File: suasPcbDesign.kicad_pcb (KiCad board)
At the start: 4 copper layers, 0 parts

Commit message: Do the layout
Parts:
- added 3xM3: MountingHole_3.2mm_M3, MountingHole:MountingHole_3.2mm_M3, F.Cu at (132.0, 186.0)
- added BBCC1: 1uF, Capacitor_SMD:C_0603_1608Metric_Pad1.08x0.95mm_HandSolder, F.Cu at (127.0, 181.2)
- added BBCC2: 1uF, Capacitor_SMD:C_0603_1608Metric_Pad1.08x0.95mm_HandSolder, F.Cu at (123.9, 181.2)
- added BBCC3: 1uF, Capacitor_SMD:C_0603_1608Metric_Pad1.08x0.95mm_HandSolder, F.Cu at (125.5, 181.2)
- added BBCC4: 0.1uF, Capacitor_SMD:C_0603_1608Metric_Pad1.08x0.95mm_HandSolder, F.Cu at (122.4, 181.2)
- added C1: 10u, Capacitor_SMD:C_0603_1608Metric_Pad1.08x0.95mm_HandSolder, F.Cu at (94.8, 102.3)
- added C2: 0.1u, Capacitor_SMD:C_0603_1608Metric_Pad1.08x0.95mm_HandSolder, F.Cu at (94.8, 98.8)
- added C3: 1u, Capacitor_SMD:C_0603_1608Metric_Pad1.08x0.95mm_HandSolder, F.Cu at (94.5, 112.9)
- added C4: 0.1u, Capacitor_SMD:C_0603_1608Metric_Pad1.08x0.95mm_HandSolder, F.Cu at (118.2, 97.8)
- added CBT1: 0.1uF, Capacitor_SMD:C_0603_1608Metric_Pad1.08x0.95mm_HandSolder, F.Cu at (119.3, 176.3)
- added CIC1: 1uF, Capacitor_SMD:C_0603_1608Metric_Pad1.08x0.95mm_HandSolder, F.Cu at (127.2, 169.5)
- added COC1: 47uF, Capacitor_SMD:C_0603_1608Metric_Pad1.08x0.95mm_HandSolder, F.Cu at (118.3, 157.5)
- added COC2: 47uF, Capacitor_SMD:C_0603_1608Metric_Pad1.08x0.95mm_HandSolder, F.Cu at (118.3, 159.3)
- added COC3: 10uF, Capacitor_SMD:C_0603_1608Metric_Pad1.08x0.95mm_HandSolder, F.Cu at (127.2, 162.9)
- added Cap1: 1uF, Capacitor_SMD:C_0603_1608Metric_Pad1.08x0.95mm_HandSolder, F.Cu at (107.8, 126.1)
- added Cap2: 0.1uF, Capacitor_SMD:C_0603_1608Metric_Pad1.08x0.95mm_HandSolder, F.Cu at (104.4, 128.8)
- added Cap3: 0.1uF, Capacitor_SMD:C_0603_1608Metric_Pad1.08x0.95mm_HandSolder, F.Cu at (102.8, 128.8)
- added Cap4: 0.1uF, Capacitor_SMD:C_0603_1608Metric_Pad1.08x0.95mm_HandSolder, F.Cu at (115.8, 128.8)
- added Cap5: 0.1uF, Capacitor_SMD:C_0603_1608Metric_Pad1.08x0.95mm_HandSolder, F.Cu at (114.1, 128.8)
- added Cap_1: 0.1uF, Capacitor_SMD:C_0603_1608Metric_Pad1.08x0.95mm_HandSolder, F.Cu at (101.1, 133.0)
- added Cap_2: 0.1uF, Capacitor_SMD:C_0603_1608Metric_Pad1.08x0.95mm_HandSolder, F.Cu at (103.1, 133.0)
- added Cap_3: 0.1uF, Capacitor_SMD:C_0603_1608Metric_Pad1.08x0.95mm_HandSolder, F.Cu at (101.1, 136.8)
- added Cap_4: 0.1uF, Capacitor_SMD:C_0603_1608Metric_Pad1.08x0.95mm_HandSolder, F.Cu at (103.1, 136.8)
- added Cap_5: 1u, Capacitor_SMD:C_0603_1608Metric_Pad1.08x0.95mm_HandSolder, F.Cu at (99.5, 158.5)
- added D1: SMF5V0A, Diode_SMD:D_SOD-123, F.Cu at (120.3, 154.8)
- added D2: LED, LED_SMD:LED_0603_1608Metric_Pad1.05x0.95mm_HandSolder, F.Cu at (126.8, 176.3)
- added D3: CUS520_H3F, Custom:USC_TOS, F.Cu at (104.0, 158.8)
- added D4: LED, LED_SMD:LED_0603_1608Metric_Pad1.05x0.95mm_HandSolder, F.Cu at (130.6, 166.7)
- added D5: LED_RGB, LED_SMD:LED_RGB_PLCC-6, F.Cu at (105.8, 164.5)
- added D6: LED, LED_SMD:LED_0603_1608Metric_Pad1.05x0.95mm_HandSolder, F.Cu at (111.0, 138.8)
- added D7: LED, LED_SMD:LED_0603_1608Metric_Pad1.05x0.95mm_HandSolder, F.Cu at (107.0, 170.5)
- added H1: BAT+, Custom:7770 Keystone Electronics PC SCREW TERMINALS, F.Cu at (95.5, 182.8)
- added H2: ESC-, Custom:MountingHole_6.3mm_M6_DIN965, F.Cu at (141.5, 96.9)
- added H3: Bat-, Custom:MountingHole_6.3mm_M6_Pad_Via, F.Cu at (141.5, 181.9)
- added J1: SENSE_IB, Connector_Wire:SolderWire-1sqmm_1x02_P5.4mm_D1.4mm_OD2.7mm, F.Cu at (91.1, 126.5)
- added J2: SPI CS, Connector_PinHeader_2.54mm:PinHeader_2x08_P2.54mm_Vertical, F.Cu at (91.0, 154.6)
- added J4: SPI CTRL, Connector_PinHeader_2.54mm:PinHeader_1x03_P2.54mm_Vertical, F.Cu at (91.0, 144.5)
- added J5: PWM CTRL, Connector_PinHeader_2.54mm:PinHeader_1x03_P2.54mm_Vertical, F.Cu at (91.0, 110.9)
- added J6: JTAG Pinout, Connector_PinHeader_2.54mm:PinHeader_1x04_P2.54mm_Vertical, F.Cu at (122.5, 137.5)
- added J7: USB_C_Receptacle_USB2.0_16P, Connector_USB:USB_C_Receptacle_GCT_USB4105-xx-A_16P_TopMnt_Horizontal, F.Cu at (109.5, 187.0)
- added JP1: VIN Vbat JPR, Jumper:SolderJumper-2_P1.3mm_Open_Pad1.0x1.5mm, F.Cu at (98.3, 154.5)
- added JP2: CS JPR, TestPoint:TestPoint_2Pads_Pitch2.54mm_Drill0.8mm, F.Cu at (117.7, 140.0)
- added JP3: S VB JPR, TestPoint:TestPoint_2Pads_Pitch2.54mm_Drill0.8mm, F.Cu at (107.5, 156.0)
- added JP3V1: 3V3 JPR, TestPoint:TestPoint_2Pads_Pitch2.54mm_Drill0.8mm, F.Cu at (126.5, 160.3)
- added JP4: VBUS JPR, TestPoint:TestPoint_2Pads_Pitch2.54mm_Drill0.8mm, F.Cu at (103.0, 172.8)
- added JP5: GNDA_GND, Jumper:SolderJumper-2_P1.3mm_Open_Pad1.0x1.5mm, F.Cu at (99.2, 123.2)
- added JP5V1: 5V JPR, TestPoint:TestPoint_2Pads_Pitch2.54mm_Drill0.8mm, F.Cu at (121.8, 158.5)
- added L1: 15uH, Inductor_SMD:L_APV_APH1050, F.Cu at (117.8, 167.3)
- added Loadcell1: Conn_01x04, Connector_PinHeader_2.54mm:PinHeader_1x04_P2.54mm_Vertical, F.Cu at (91.0, 139.4)
- added R1: 100, Resistor_SMD:R_0603_1608Metric_Pad0.98x0.95mm_HandSolder, F.Cu at (96.8, 128.0)
- added R10: 10, Resistor_SMD:R_0603_1608Metric_Pad0.98x0.95mm_HandSolder, F.Cu at (115.4, 131.2)
- added R11: 10, Resistor_SMD:R_0603_1608Metric_Pad0.98x0.95mm_HandSolder, F.Cu at (115.4, 132.8)
- added R12: 10, Resistor_SMD:R_0603_1608Metric_Pad0.98x0.95mm_HandSolder, F.Cu at (115.4, 134.5)
- added R13: 10, Resistor_SMD:R_0603_1608Metric_Pad0.98x0.95mm_HandSolder, F.Cu at (115.4, 136.1)
- added R14: 10, Resistor_SMD:R_0603_1608Metric_Pad0.98x0.95mm_HandSolder, F.Cu at (115.4, 137.7)
- added R15: 50R, Resistor_SMD:R_0603_1608Metric_Pad0.98x0.95mm_HandSolder, F.Cu at (130.6, 163.3)
- added R16: 5.1k, Resistor_SMD:R_0603_1608Metric_Pad0.98x0.95mm_HandSolder, F.Cu at (103.0, 122.2)
- added R17: 25R, Resistor_SMD:R_0603_1608Metric_Pad0.98x0.95mm_HandSolder, F.Cu at (99.0, 168.0)
- added R18: 25R, Resistor_SMD:R_0603_1608Metric_Pad0.98x0.95mm_HandSolder, F.Cu at (100.8, 168.0)
- added R19: 75R, Resistor_SMD:R_0603_1608Metric_Pad0.98x0.95mm_HandSolder, F.Cu at (102.5, 168.0)
- added R2: 100, Resistor_SMD:R_0603_1608Metric_Pad0.98x0.95mm_HandSolder, F.Cu at (96.8, 125.8)
- added R20: 5.1k, Resistor_SMD:R_0603_1608Metric_Pad0.98x0.95mm_HandSolder, F.Cu at (106.8, 122.2)
- added R21: 200R, Resistor_SMD:R_0603_1608Metric_Pad0.98x0.95mm_HandSolder, F.Cu at (108.0, 138.8)
- added R22: 5.1k, Resistor_SMD:R_0603_1608Metric_Pad0.98x0.95mm_HandSolder, F.Cu at (105.2, 179.5)
- added R23: 5.1k, Resistor_SMD:R_0603_1608Metric_Pad0.98x0.95mm_HandSolder, F.Cu at (113.5, 179.5)
- added R24: 10k, Resistor_SMD:R_0603_1608Metric_Pad0.98x0.95mm_HandSolder, F.Cu at (112.5, 175.0)
- added R25: 200R, Resistor_SMD:R_0603_1608Metric_Pad0.98x0.95mm_HandSolder, F.Cu at (111.0, 170.5)
- added R26: 10k, Resistor_SMD:R_0603_1608Metric_Pad0.98x0.95mm_HandSolder, F.Cu at (94.5, 109.5)
- added R3: 100, Resistor_SMD:R_0603_1608Metric_Pad0.98x0.95mm_HandSolder, F.Cu at (96.8, 132.3)
- added R4: 100, Resistor_SMD:R_0603_1608Metric_Pad0.98x0.95mm_HandSolder, F.Cu at (96.8, 130.2)
- added R5: 10, Resistor_SMD:R_0603_1608Metric_Pad0.98x0.95mm_HandSolder, F.Cu at (101.1, 128.8)
- added R6: 200R, Resistor_SMD:R_0603_1608Metric_Pad0.98x0.95mm_HandSolder, F.Cu at (126.8, 173.0)
- added R7: 36k, Resistor_SMD:R_0603_1608Metric_Pad0.98x0.95mm_HandSolder, F.Cu at (95.0, 150.0)
- added R8: 4k, Resistor_SMD:R_0603_1608Metric_Pad0.98x0.95mm_HandSolder, F.Cu at (95.0, 143.5)
- added R9: 10, Resistor_SMD:R_0603_1608Metric_Pad0.98x0.95mm_HandSolder, F.Cu at (117.4, 128.8)
- added REF**: MountingHole_3.2mm_M3, MountingHole:MountingHole_3.2mm_M3, F.Cu at (132.0, 94.0)
- added REF**: MountingHole_3.2mm_M3, MountingHole:MountingHole_3.2mm_M3, F.Cu at (90.2, 94.0)
- added RFB1: 100k, Resistor_SMD:R_0603_1608Metric_Pad0.98x0.95mm_HandSolder, F.Cu at (119.5, 180.0)
- added RFB2: 19.2k, Resistor_SMD:R_0603_1608Metric_Pad0.98x0.95mm_HandSolder, F.Cu at (119.5, 181.8)
- added RV1: 20k, Potentiometer_THT:Potentiometer_Bourns_3386P_Vertical, F.Cu at (102.0, 149.0)
- added SW1: SW_SPST, Button_Switch_THT:SW_PUSH_1P1T_6x3.5mm_H4.3_APEM_MJTP1243, F.Cu at (127.2, 118.8)
- added SW2: SW_SPST, Button_Switch_THT:SW_PUSH_1P1T_6x3.5mm_H4.3_APEM_MJTP1243, F.Cu at (126.2, 122.5)
- added SW3: SW_SPST, Button_Switch_THT:SW_PUSH_1P1T_6x3.5mm_H4.3_APEM_MJTP1243, F.Cu at (126.5, 108.5)
- added SW4: SW_SPST, Button_Switch_THT:SW_PUSH_1P1T_6x3.5mm_H4.3_APEM_MJTP1243, F.Cu at (123.0, 118.8)
- added SW5: SW_SPST, Button_Switch_THT:SW_PUSH_1P1T_6x3.5mm_H4.3_APEM_MJTP1243, F.Cu at (118.5, 118.8)
- added SW6: SW_SPST, Button_Switch_THT:SW_PUSH_1P1T_6x3.5mm_H4.3_APEM_MJTP1243, F.Cu at (91.2, 106.0)
- added SW7: SW_SPST, Button_Switch_THT:SW_PUSH_1P1T_6x3.5mm_H4.3_APEM_MJTP1243, F.Cu at (120.0, 101.2)
- added U1: 74HC138, Package_SO:TSSOP-16_4.4x5mm_P0.65mm, F.Cu at (119.5, 146.5)
- added U2: LMR51625DDC, Package_TO_SOT_SMD:TSOT-23-6_HandSoldering, F.Cu at (122.0, 176.3)
- added U3: MCP3562RT-E/ST, Package_SO:TSSOP-20_4.4x6.5mm_P0.65mm, F.Cu at (109.2, 132.2)
- added U4: ~, Package_TO_SOT_SMD:SOT-23-5_HandSoldering, F.Cu at (103.5, 154.8)
- added U5: TLV77733PDBVR, Package_TO_SOT_SMD:SOT-23-5_HandSoldering, F.Cu at (127.4, 166.2)
- added U6: LMV331, Package_TO_SOT_SMD:SOT-23-5_HandSoldering, F.Cu at (113.2, 121.2)
- added U7: ESP32-S3-WROOM-1, RF_Module:ESP32-S3-WROOM-1, F.Cu at (105.7, 103.5)
- added U8: LM66100DCK, Package_TO_SOT_SMD:SOT-363_SC-70-6, F.Cu at (106.0, 175.0)
- added U9: USBLC6-2SC6, Package_TO_SOT_SMD:SOT-23-6, F.Cu at (109.4, 178.7)
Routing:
- net 5V: track 0.00 -> 147.9 mm, vias 0 -> 10
- net /SPI_CC1: track 0.00 -> 126.7 mm, vias 0 -> 6
- net /SPI_CC2: track 0.00 -> 126.6 mm, vias 0 -> 6
- net /SPI_CC0: track 0.00 -> 98.2 mm, vias 0 -> 5
- net GND: track 0.00 -> 86.7 mm, vias 0 -> 29
- net /USB_D_N: track 0.00 -> 86.7 mm, vias 0 -> 2
- net /USB_D_P: track 0.00 -> 85.5 mm, vias 0 -> 2
- net /IND_B: track 0.00 -> 78.2 mm, vias 0 -> 4
- net /IND_G: track 0.00 -> 75.1 mm, vias 0 -> 4
- net /IND_R: track 0.00 -> 68.0 mm, vias 0 -> 4
- net /SPI_MISO: track 0.00 -> 67.0 mm, vias 0 -> 5
- net /SENSE_VB: track 0.00 -> 64.7 mm, vias 0 -> 2
- net /VIN: track 0.00 -> 63.4 mm, vias 0 -> 2
- net /SPI_SCLK: track 0.00 -> 63.3 mm, vias 0 -> 4
- net /SPI_MOSI: track 0.00 -> 61.9 mm, vias 0 -> 5
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- added copper zone on F.Cu, net /VIN
- added copper zone on F.Cu, net 5V
- added copper zone on F.Cu, net GND
- added copper zone on In1.Cu, net GND
- added copper zone on F.Cu, net GNDA
- added copper zone on F.Cu, net Net-(U2-SW)
- added copper zone on F.Cu, net VDD
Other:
- board outline added: 66.8 x 100.1 mm
- board text added: "+ -"
- board text added: "-+C"
- board text added: "0 <- CS -> 7"
- board text added: "BOOT"
- board text added: "CK MI MO"
- board text added: "CS SRC"
- board text added: "E+ E- A+ A-"
- board text added: "JP3v3"
- board text added: "JP5V"
- board text added: "RST"
- board text added: "VBUS"

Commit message: Add logo
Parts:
- added G***: LOGO, Custom:UMBC_Footprint_Official_Large, F.Cu at (141.5, 138.4)

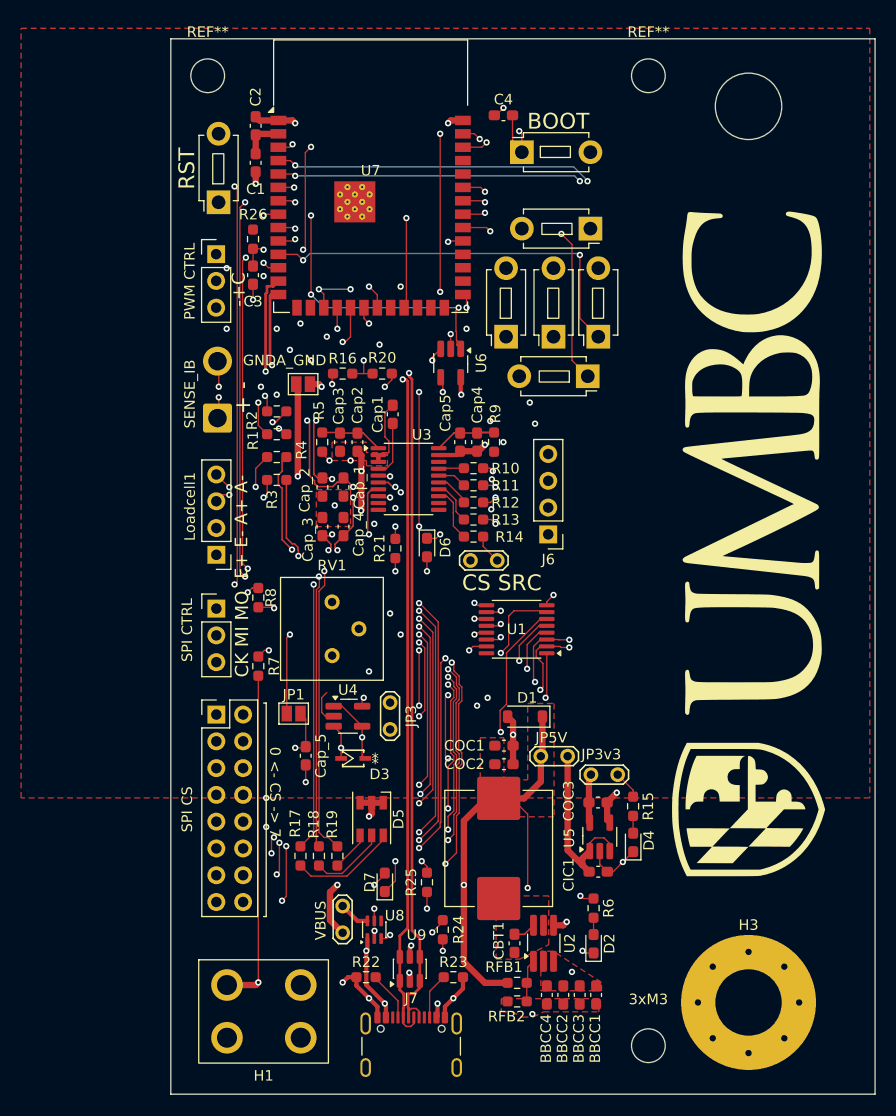
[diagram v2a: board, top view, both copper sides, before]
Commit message: Change to 4 mounting hole design
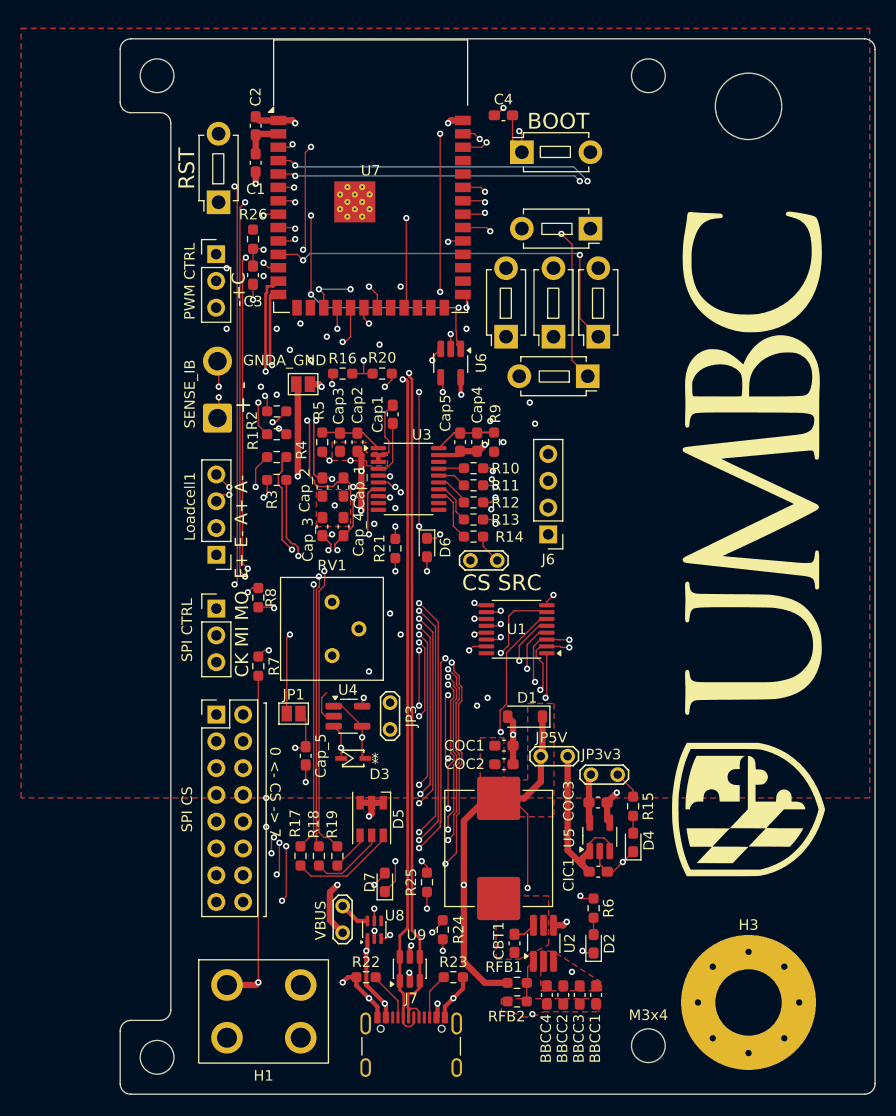
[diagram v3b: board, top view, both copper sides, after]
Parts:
- added M3x1: MountingHole_3.2mm_M3, MountingHole:MountingHole_3.2mm_M3, F.Cu at (85.4, 187.1)
- moved M3x2 4.80 mm to (85.4, 94.0)
- renumbered REF** to M3x2, REF** to M3x3, 3xM3 to M3x4
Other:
- board size 66.8 x 100.1 mm -> 71.6 x 100.1 mm

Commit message: Add Battery and ESC negative terminal labels
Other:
- board text added: "BAT -"
- board text added: "ESC -"
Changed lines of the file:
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@@
 			(at 0 -7.35 0)
 			(layer "F.SilkS")
+			(hide yes)
 			(effects
 				(font
@@
 		(layer "F.SilkS")
 		(effects
+			(font
+				(size 1 1)
+				(thickness 0.15)
+			)
+			(justify left bottom)
+		)
+	)
+	(gr_text "ESC -"
+		(at 139.6 102.5 0)
+		(layer "F.SilkS")
+		(effects
+			(font
+				(size 1 1)
+				(thickness 0.15)
+			)
+			(justify left bottom)
+		)
+	)
+	(gr_text "BAT -"
+		(at 140 174.7 0)
+		(layer "F.SilkS")
+		(effects

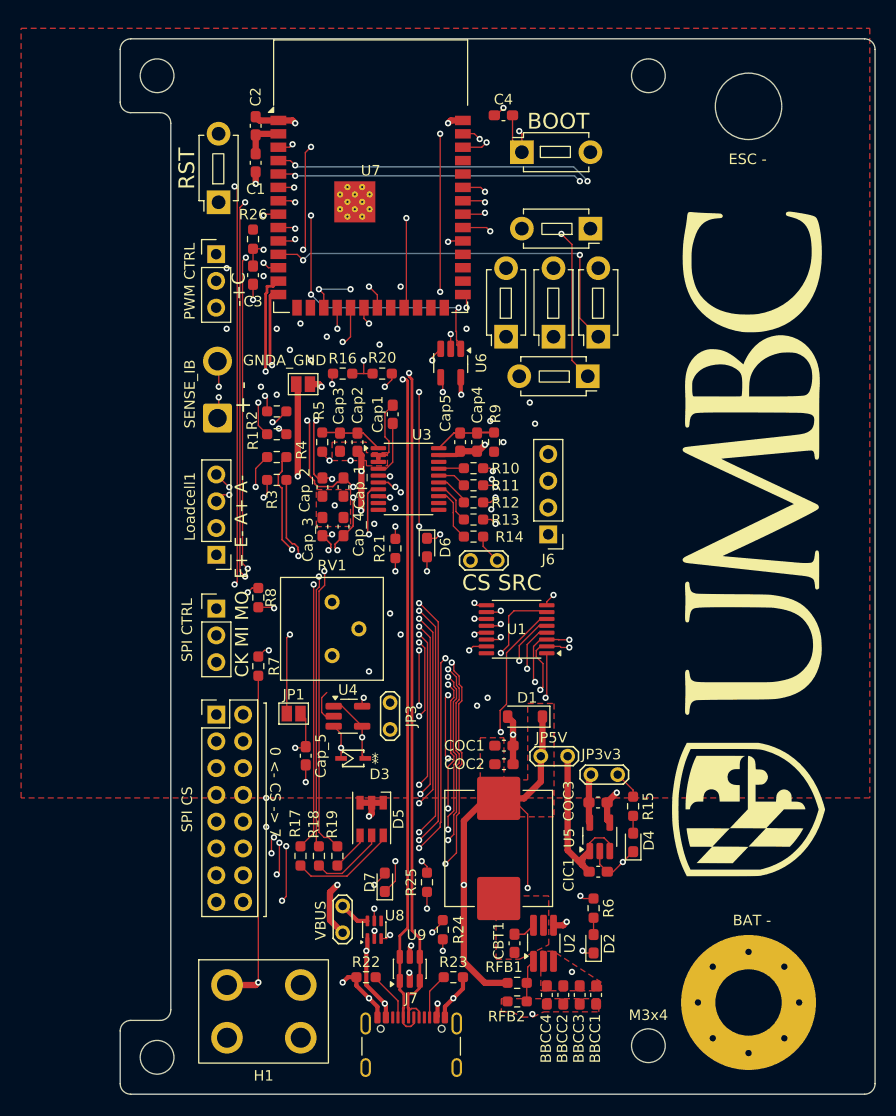
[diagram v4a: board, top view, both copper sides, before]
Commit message: Update to use tht led
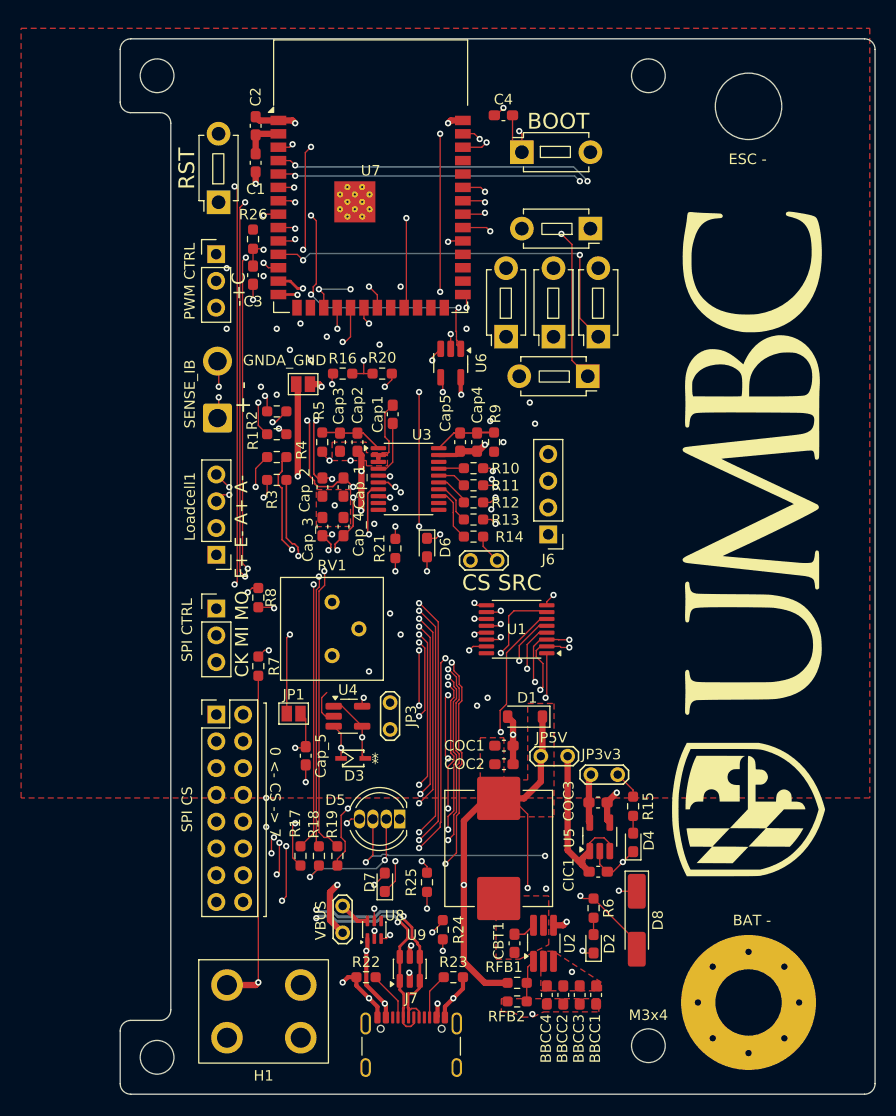
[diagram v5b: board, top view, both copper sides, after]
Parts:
- added D8: D, Diode_SMD:D_MiniMELF_Handsoldering, F.Cu at (130.9, 174.1)
- D5: value LED_RGB -> LED IND; footprint LED_SMD:LED_RGB_PLCC-6 -> LED_THT:LED_D5.0mm-4_RGB
- R17, R18: value 25R -> 62R
- R19: value 75R -> 110R
- moved D5 2.66 mm to (108.4, 164.5), turned to 180 degrees
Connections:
- D5 pad 1: GND -> Net-(D5-BK)
- D5 pad 2: GND -> Net-(D5-GK)
- D5 pad 3: GND -> Net-(D5-A)
- D5 pad 4: Net-(D5-BA) -> Net-(D5-RK)
- R17 pad 2: Net-(D5-RA) -> Net-(D5-RK)
- R18 pad 2: Net-(D5-GA) -> Net-(D5-GK)
- R19 pad 2: Net-(D5-BA) -> Net-(D5-BK)
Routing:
- net Net-(D5-A): track 0.00 -> 33.6 mm, vias 0 -> 4
- net Net-(D5-GK): track 0.00 -> 13.2 mm, vias 0 -> 2
- net Net-(D5-BK): track 0.00 -> 11.8 mm, vias 0 -> 1
- net Net-(D5-RK): track 0.00 -> 11.0 mm, vias 0 -> 2
- net Net-(D5-RA): track 10.1 -> 0.00 mm
- net Net-(D5-GA): track 7.29 -> 0.00 mm
- net 5V: track 147.9 -> 154.4 mm
- net Net-(D5-BA): track 3.75 -> 0.00 mm
- net GND: track 86.7 -> 83.1 mm, vias 29 -> 28
- net /SPI_CC1: track 126.7 -> 127.8 mm
- net /USB_D_P: track 85.5 -> 86.3 mm, vias 2 -> 3
- net /USB_D_N: track 86.7 -> 87.4 mm, vias 2 -> 3
- net /SPI_PR6: track 50.2 -> 50.8 mm

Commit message: Fix PCB size
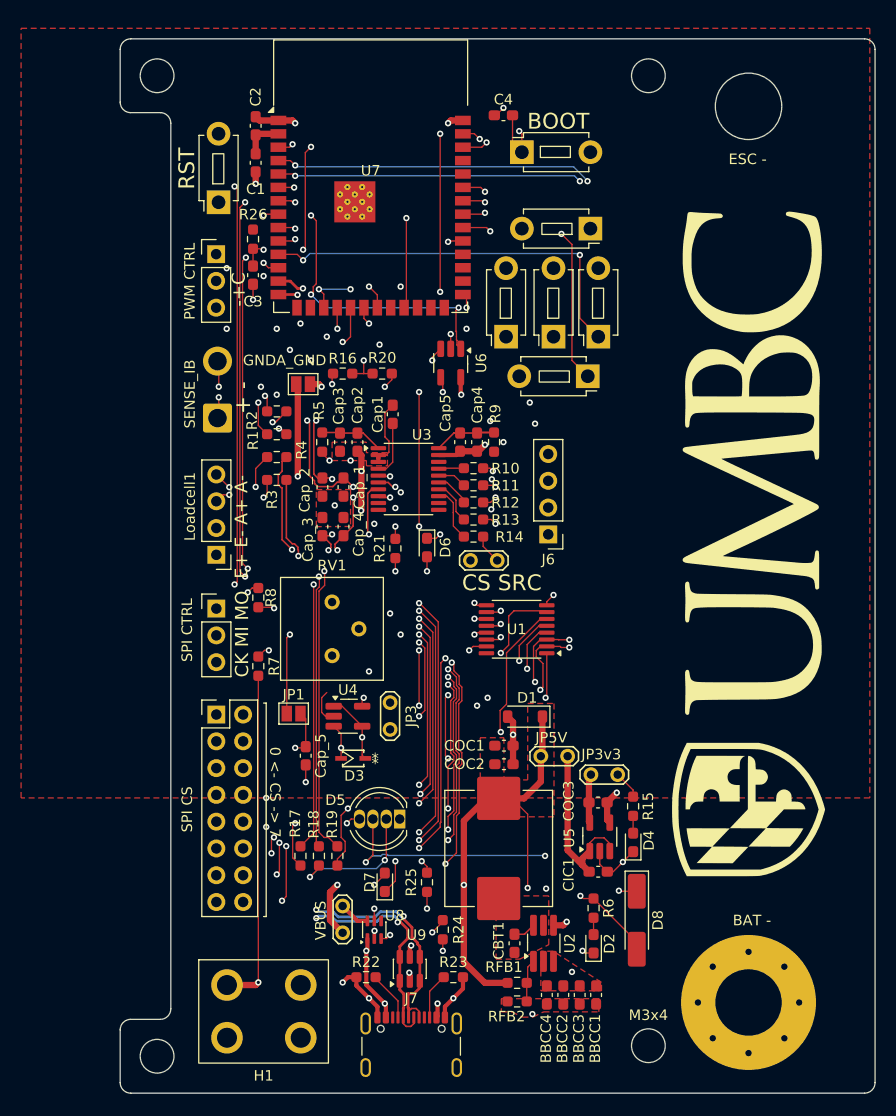
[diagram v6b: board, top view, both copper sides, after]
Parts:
- moved M3x1 0.10 mm to (85.4, 187.0)
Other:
- board size 71.6 x 100.1 mm -> 71.6 x 100 mm
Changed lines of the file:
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@@
 		)
 		(pad_to_mask_clearance 0)
-		(solder_mask_min_width 0.12)
 		(allow_soldermask_bridges_in_footprints no)
 		(tenting
@@
 	(footprint "MountingHole:MountingHole_3.2mm_M3"
 		(layer "F.Cu")
-		(at 85.4 187.1)
+		(at 85.4 187)
 		(descr "Mounting Hole 3.2mm, M3, no annular, generated by kicad-footprint-generator mountinghole.py")
 		(tags "mountinghole M3")
@@
 	)
 	(gr_arc
-		(start 81.9 184.6)
-		(mid 82.192893 183.892893)
-		(end 82.9 183.6)
+		(start 81.9 184.5)
+		(mid 82.192893 183.792893)
+		(end 82.9 183.5)
 		(stroke
 			(width 0.05)
@@
 	)
 	(gr_line
-		(start 81.9 189.6)
-		(end 81.9 184.6)
+		(start 81.9 189.5)
+		(end 81.9 184.5)
 		(stroke
 			(width 0.05)
@@
 	)
 	(gr_line
-		(start 82.9 183.6)
-		(end 85.7 183.6)
+		(start 82.9 183.5)
+		(end 85.7 183.5)
 		(stroke
 			(width 0.05)
@@
 	)
 	(gr_arc
-		(start 82.9 190.6)
-		(mid 82.192893 190.307107)
-		(end 81.9 189.6)
+		(start 82.9 190.5)
+		(mid 82.192893 190.207107)
+		(end 81.9 189.5)
 		(stroke
 			(width 0.05)
@@
 	)
 	(gr_line
-		(start 82.9 190.6)
-		(end 152.5 190.6)
+		(start 82.9 190.5)
+		(end 152.5 190.5)
 		(stroke
 			(width 0.05)
@@
 	(gr_line
 		(start 86.7 98.5)
-		(end 86.7 182.6)
+		(end 86.7 182.5)
 		(stroke
 			(width 0.05)
@@
 	)
 	(gr_arc
-		(start 86.7 182.6)
-		(mid 86.407107 183.307107)
-		(end 85.7 183.6)
+		(start 86.7 182.5)
+		(mid 86.407107 183.207107)
+		(end 85.7 183.5)
 		(stroke
 			(width 0.05)
@@
 	)
 	(gr_arc
-		(start 153.5 189.6)
-		(mid 153.207107 190.307107)
-		(end 152.5 190.6)
+		(start 153.5 189.5)
+		(mid 153.207107 190.207107)
+		(end 152.5 190.5)
 		(stroke
 			(width 0.05)
@@
 	)
 	(gr_line
-		(start 153.5 189.6)
+		(start 153.5 189.5)
 		(end 153.5 91.5)
 		(stroke
@@
 		(members "22de6458-355f-4f17-bb94-1a58c7a894bf" "73150530-0241-4595-bf58-92723f993fa7")
 	)
-	(group ""
-		(members "5baa84fb-138e-4b9c-8745-a987d2dac32e" "b192e089-6447-41c8-8f59-4d895d3663ee"
-			"d56a1cfd-bb69-47e3-97c7-ac4e348aef2f"
-		)
-	)
 	(embedded_fonts no)
